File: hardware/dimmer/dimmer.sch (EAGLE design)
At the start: 34 parts, among them IC1 MEGA48/88/168-PU, IC2 RFM12, IC3 7812L, IC4 LP2950Z, K1 G5LE, T1 BC547, T2 BC547, X1 AC In, X2 DIM Out, X3 AC Out

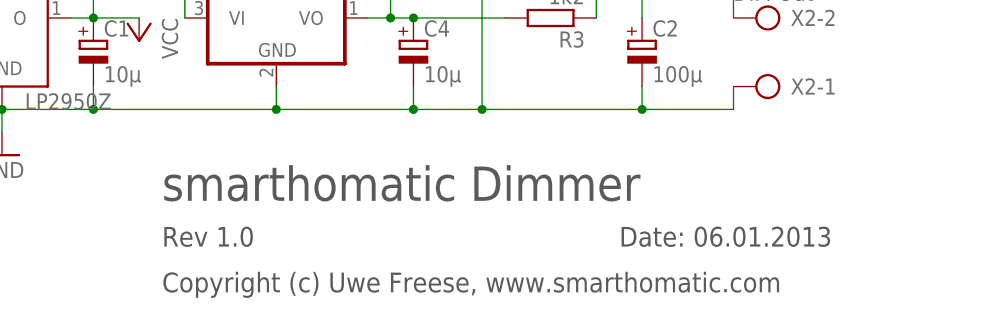
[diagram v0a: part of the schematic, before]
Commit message: use .org domain
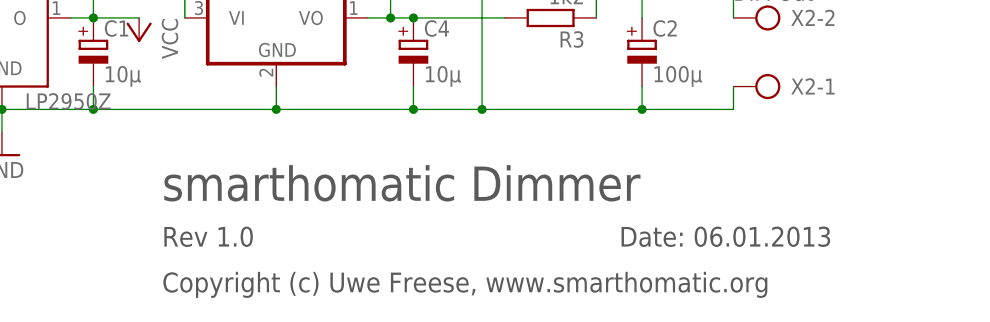
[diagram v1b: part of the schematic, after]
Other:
- note added: "Copyright (c) Uwe Freese, www.smarthomatic.org"
- note removed: "Copyright (c) Uwe Freese, www.smarthomatic.com"
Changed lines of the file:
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@@
 <text x="63.5" y="-81.28" size="2.1844" layer="97">Date: 06.01.2013</text>
 <text x="12.7" y="-81.28" size="2.1844" layer="97">Rev 1.0</text>
-<text x="12.7" y="-86.36" size="2.1844" layer="97">Copyright (c) Uwe Freese, www.smarthomatic.com</text>
+<text x="12.7" y="-86.36" size="2.1844" layer="97">Copyright (c) Uwe Freese, www.smarthomatic.org</text>
 </plain>
 <instances>

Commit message: update labels
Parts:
- D1, D2, D3, D4, D5, D6: value 1N4148DO35-7 -> 1N4148
- JP3: value TX -> PD1/TX
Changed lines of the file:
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@@
 <part name="JP5" library="pinhead" deviceset="PINHD-1X1" device="" value="ANT"/>
 <part name="TR1" library="trafo" deviceset="EE20-1" device="" value="12V"/>
-<part name="D1" library="diode" deviceset="1N4148" device="DO35-7"/>
-<part name="D2" library="diode" deviceset="1N4148" device="DO35-7"/>
-<part name="D3" library="diode" deviceset="1N4148" device="DO35-7"/>
-<part name="D4" library="diode" deviceset="1N4148" device="DO35-7"/>
+<part name="D1" library="diode" deviceset="1N4148" device="DO35-7" value="1N4148"/>
+<part name="D2" library="diode" deviceset="1N4148" device="DO35-7" value="1N4148"/>
+<part name="D3" library="diode" deviceset="1N4148" device="DO35-7" value="1N4148"/>
+<part name="D4" library="diode" deviceset="1N4148" device="DO35-7" value="1N4148"/>
 <part name="IC3" library="linear" deviceset="78*" device="L" technology="12"/>
 <part name="P+4" library="supply1" deviceset="VCC" device=""/>
@@
 <part name="X1" library="con-ptr500" deviceset="AK500/2" device="" value="AC In"/>
 <part name="X2" library="con-ptr500" deviceset="AK500/2" device="" value="DIM Out"/>
-<part name="D5" library="diode" deviceset="1N4148" device="DO35-7"/>
-<part name="D6" library="diode" deviceset="1N4148" device="DO35-7"/>
+<part name="D5" library="diode" deviceset="1N4148" device="DO35-7" value="1N4148"/>
+<part name="D6" library="diode" deviceset="1N4148" device="DO35-7" value="1N4148"/>
 <part name="C4" library="rcl" deviceset="CPOL-EU" device="E1.8-4" value="10µ"/>
 <part name="C3" library="rcl" deviceset="C-EU" device="025-030X050" value="220n"/>
@@
 <part name="R6" library="rcl" deviceset="R-EU_" device="0207/7" value="1k"/>
 <part name="JP2" library="pinhead" deviceset="PINHD-1X2" device="" value="POWER"/>
-<part name="JP3" library="pinhead" deviceset="PINHD-1X1" device="" value="TX"/>
+<part name="JP3" library="pinhead" deviceset="PINHD-1X1" device="" value="PD1/TX"/>
 <part name="JP4" library="pinhead" deviceset="PINHD-1X2" device="" value="On/Off"/>
 <part name="GND4" library="supply1" deviceset="GND" device=""/>

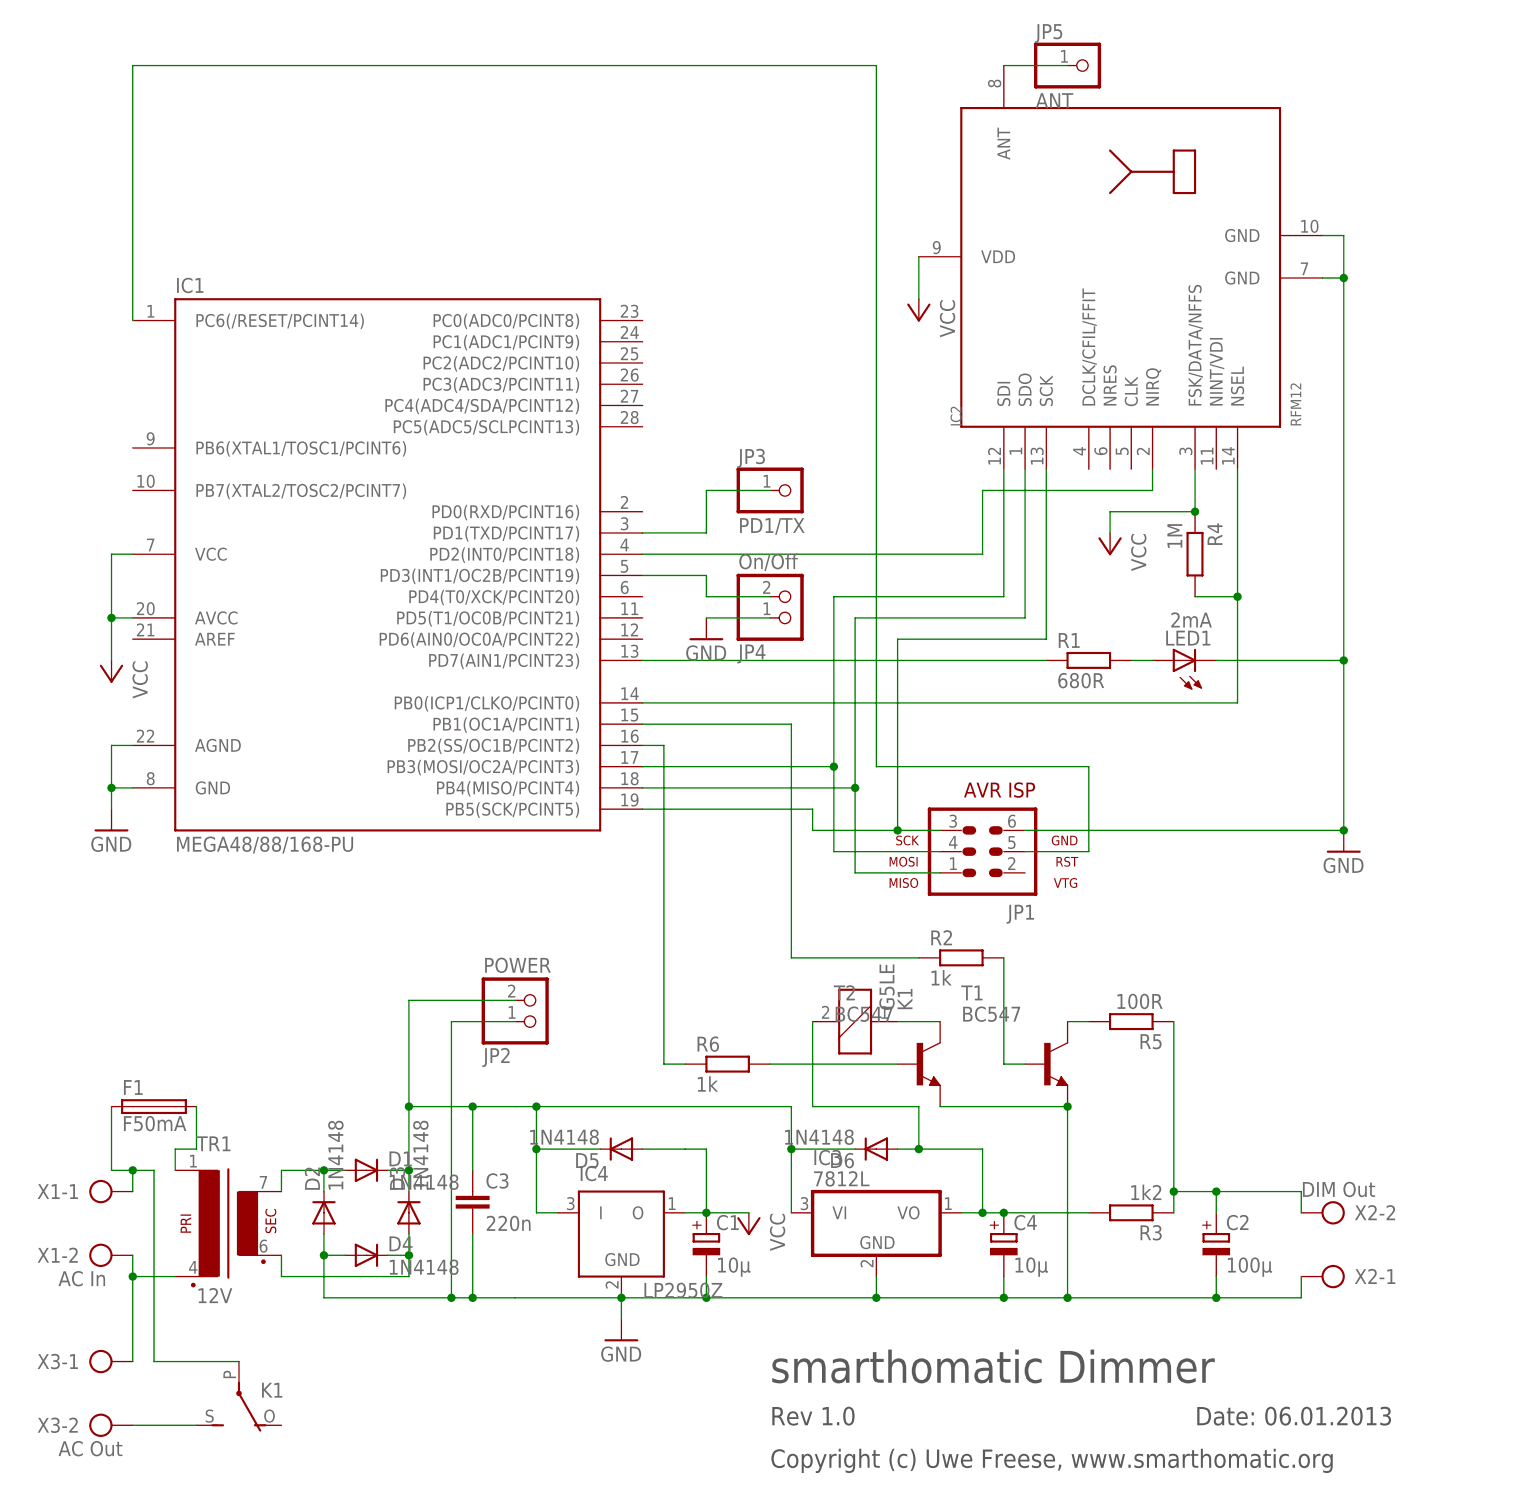
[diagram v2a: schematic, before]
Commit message: Use 1k3 instead of 1k2 resistor (0,1%), which is more common. Adopt lookup table accordingly. Change power off timeout to 3s.
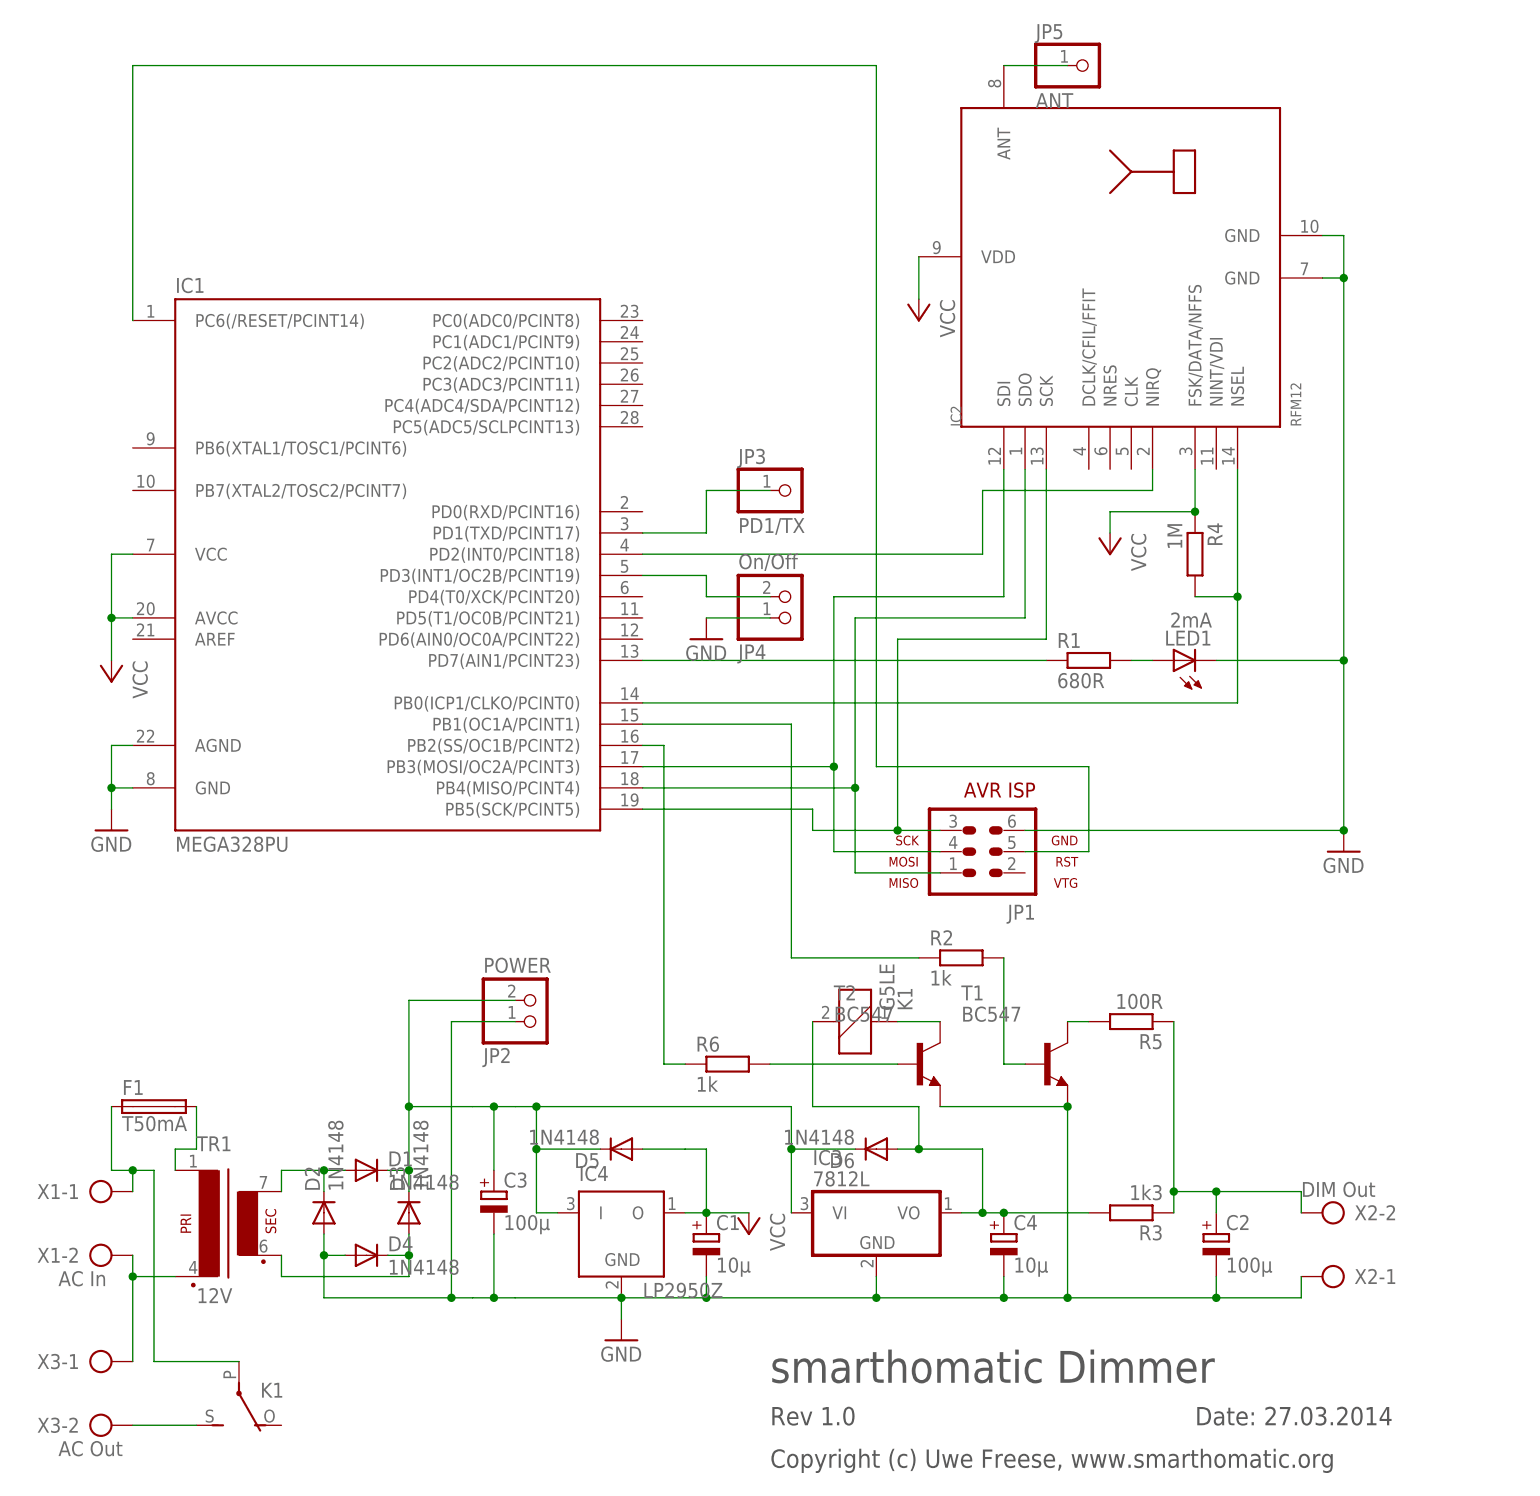
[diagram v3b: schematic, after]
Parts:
- C3: value 220n -> 100µ; device rcl:C-EU025-030X050 -> rcl:CPOL-EUE1.8-4
- F1: value F50mA -> T50mA; device fuse:GSH15 -> fuse:SH22,5
- IC1: value MEGA48/88/168-PU -> MEGA328PU
- R3: value 1k2 -> 1k3
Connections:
- net GND: now also C3.-; no longer C3.2
- net N$9: now also C3.+; no longer C3.1
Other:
- note added: "Date: 27.03.2014"
- note removed: "Date: 06.01.2013"
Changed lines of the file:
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@@
 <part name="IC2" library="hopeRF" deviceset="RFM12" device=""/>
 <part name="LED1" library="led" deviceset="LED" device="3MM" value="2mA"/>
-<part name="IC1" library="avr-5-4.16" deviceset="MEGA48/88/168-PU" device=""/>
+<part name="IC1" library="avr-5-4.16" deviceset="MEGA48/88/168-PU" device="" value="MEGA328PU"/>
 <part name="JP1" library="avr-5-4.16" deviceset="AVR-ISP-6" device=""/>
 <part name="P+1" library="supply1" deviceset="VCC" device=""/>
@@
 <part name="R2" library="rcl" deviceset="R-EU_" device="0207/7" value="1k"/>
 <part name="IC4" library="linear" deviceset="LP2950" device="Z"/>
-<part name="R3" library="rcl" deviceset="R-EU_" device="0207/7" value="1k2"/>
+<part name="R3" library="rcl" deviceset="R-EU_" device="0207/7" value="1k3"/>
 <part name="R5" library="rcl" deviceset="R-EU_" device="0207/7" value="100R"/>
 <part name="C2" library="rcl" deviceset="CPOL-EU" device="E1.8-4" value="100µ"/>
@@
 <part name="D6" library="diode" deviceset="1N4148" device="DO35-7" value="1N4148"/>
 <part name="C4" library="rcl" deviceset="CPOL-EU" device="E1.8-4" value="10µ"/>
-<part name="C3" library="rcl" deviceset="C-EU" device="025-030X050" value="220n"/>
 <part name="X3" library="con-ptr500" deviceset="AK500/2" device="" value="AC Out">
 <attribute name="MF" value=""/>
@@
 </part>
 <part name="K1" library="relay" deviceset="G5LE" device=""/>
-<part name="F1" library="fuse" deviceset="GSH15" device="" value="F50mA"/>
 <part name="T2" library="transistor" deviceset="BC547" device=""/>
 <part name="R6" library="rcl" deviceset="R-EU_" device="0207/7" value="1k"/>
@@
 <part name="JP4" library="pinhead" deviceset="PINHD-1X2" device="" value="On/Off"/>
 <part name="GND4" library="supply1" deviceset="GND" device=""/>
+<part name="F1" library="fuse" deviceset="SH22,5" device="" value="T50mA"/>
+<part name="C3" library="rcl" deviceset="CPOL-EU" device="E1.8-4" value="100µ"/>
 </parts>
 <sheets>
@@
 <frame x1="-81.28" y1="-104.14" x2="99.06" y2="91.44" columns="8" rows="5" layer="97"/>
 <text x="12.7" y="-76.2" size="3.81" layer="97">smarthomatic Dimmer</text>
-<text x="63.5" y="-81.28" size="2.1844" layer="97">Date: 06.01.2013</text>
+<text x="63.5" y="-81.28" size="2.1844" layer="97">Date: 27.03.2014</text>
 <text x="12.7" y="-81.28" size="2.1844" layer="97">Rev 1.0</text>
 <text x="12.7" y="-86.36" size="2.1844" layer="97">Copyright (c) Uwe Freese, www.smarthomatic.org</text>
@@
 <instance part="D6" gate="G$1" x="25.4" y="-48.26" rot="R180"/>
 <instance part="C4" gate="G$1" x="40.64" y="-58.42"/>
-<instance part="C3" gate="G$1" x="-22.86" y="-53.34"/>
 <instance part="X3" gate="-1" x="-68.58" y="-73.66"/>
 <instance part="X3" gate="-2" x="-68.58" y="-81.28"/>
 <instance part="K1" gate="1" x="22.86" y="-33.02" rot="MR90"/>
 <instance part="K1" gate="2" x="-50.8" y="-76.2" rot="MR180"/>
-<instance part="F1" gate="1" x="-60.96" y="-43.18"/>
 <instance part="T2" gate="G$1" x="30.48" y="-38.1"/>
 <instance part="R6" gate="G$1" x="7.62" y="-38.1"/>
@@
 <instance part="JP4" gate="G$1" x="15.24" y="17.78" rot="MR180"/>
 <instance part="GND4" gate="1" x="5.08" y="12.7"/>
+<instance part="F1" gate="1" x="-60.96" y="-43.18"/>
+<instance part="C3" gate="G$1" x="-20.32" y="-53.34"/>
 </instances>
 <busses>
@@
 <wire x1="5.08" y1="-66.04" x2="-5.08" y2="-66.04" width="0.1524" layer="91"/>
 <wire x1="-5.08" y1="-66.04" x2="-17.78" y2="-66.04" width="0.1524" layer="91"/>
-<wire x1="-17.78" y1="-66.04" x2="-22.86" y2="-66.04" width="0.1524" layer="91"/>
+<wire x1="-17.78" y1="-66.04" x2="-20.32" y2="-66.04" width="0.1524" layer="91"/>
+<wire x1="-20.32" y1="-66.04" x2="-22.86" y2="-66.04" width="0.1524" layer="91"/>
 <wire x1="-22.86" y1="-66.04" x2="-25.4" y2="-66.04" width="0.1524" layer="91"/>
 <wire x1="-25.4" y1="-66.04" x2="-40.64" y2="-66.04" width="0.1524" layer="91"/>
@@
 <wire x1="5.08" y1="-66.04" x2="5.08" y2="-63.5" width="0.1524" layer="91"/>
 <junction x="5.08" y="-66.04"/>
-<pinref part="C3" gate="G$1" pin="2"/>
-<wire x1="-22.86" y1="-58.42" x2="-22.86" y2="-66.04" width="0.1524" layer="91"/>
-<junction x="-22.86" y="-66.04"/>
 <pinref part="T2" gate="G$1" pin="E"/>
 <wire x1="33.02" y1="-43.18" x2="48.26" y2="-43.18" width="0.1524" layer="91"/>
@@
 <pinref part="JP2" gate="G$1" pin="1"/>
 <wire x1="-25.4" y1="-33.02" x2="-17.78" y2="-33.02" width="0.1524" layer="91"/>
+<pinref part="C3" gate="G$1" pin="-"/>
+<wire x1="-20.32" y1="-58.42" x2="-20.32" y2="-66.04" width="0.1524" layer="91"/>
+<junction x="-20.32" y="-66.04"/>
 </segment>
 <segment>
@@
 <pinref part="IC3" gate="A1" pin="VI"/>
 <wire x1="-30.48" y1="-43.18" x2="-22.86" y2="-43.18" width="0.1524" layer="91"/>
-<wire x1="-22.86" y1="-43.18" x2="-17.78" y2="-43.18" width="0.1524" layer="91"/>
+<wire x1="-22.86" y1="-43.18" x2="-20.32" y2="-43.18" width="0.1524" layer="91"/>
+<wire x1="-20.32" y1="-43.18" x2="-17.78" y2="-43.18" width="0.1524" layer="91"/>
 <wire x1="-17.78" y1="-43.18" x2="-15.24" y2="-43.18" width="0.1524" layer="91"/>
 <wire x1="-15.24" y1="-43.18" x2="15.24" y2="-43.18" width="0.1524" layer="91"/>
@@
 <wire x1="22.86" y1="-48.26" x2="15.24" y2="-48.26" width="0.1524" layer="91"/>
 <junction x="15.24" y="-48.26"/>
-<pinref part="C3" gate="G$1" pin="1"/>
-<wire x1="-22.86" y1="-50.8" x2="-22.86" y2="-43.18" width="0.1524" layer="91"/>
-<junction x="-22.86" y="-43.18"/>
 <wire x1="-30.48" y1="-43.18" x2="-30.48" y2="-30.48" width="0.1524" layer="91"/>
 <junction x="-30.48" y="-43.18"/>
 <pinref part="JP2" gate="G$1" pin="2"/>
 <wire x1="-30.48" y1="-30.48" x2="-17.78" y2="-30.48" width="0.1524" layer="91"/>
+<pinref part="C3" gate="G$1" pin="+"/>
+<wire x1="-20.32" y1="-43.18" x2="-20.32" y2="-50.8" width="0.1524" layer="91"/>
+<junction x="-20.32" y="-43.18"/>
 </segment>
 </net>
@@
 <segment>
 <wire x1="-63.5" y1="-50.8" x2="-66.04" y2="-50.8" width="0.1524" layer="91"/>
-<pinref part="F1" gate="1" pin="1"/>
-<wire x1="-66.04" y1="-50.8" x2="-66.04" y2="-43.18" width="0.1524" layer="91"/>
 <wire x1="-63.5" y1="-50.8" x2="-60.96" y2="-50.8" width="0.1524" layer="91"/>
 <pinref part="K1" gate="2" pin="P"/>
@@
 <wire x1="-63.5" y1="-53.34" x2="-63.5" y2="-50.8" width="0.1524" layer="91"/>
 <junction x="-63.5" y="-50.8"/>
+<pinref part="F1" gate="1" pin="1"/>
+<wire x1="-66.04" y1="-50.8" x2="-66.04" y2="-43.18" width="0.1524" layer="91"/>
 </segment>
 </net>
 <net name="N$23" class="0">
 <segment>
-<pinref part="F1" gate="1" pin="2"/>
-<wire x1="-55.88" y1="-43.18" x2="-55.88" y2="-48.26" width="0.1524" layer="91"/>
 <wire x1="-55.88" y1="-48.26" x2="-58.42" y2="-48.26" width="0.1524" layer="91"/>
 <pinref part="TR1" gate="1" pin="P1"/>
 <wire x1="-58.42" y1="-48.26" x2="-58.42" y2="-50.8" width="0.1524" layer="91"/>
-</segment>
-</net>
+<pinref part="F1" gate="1" pin="2"/>
+<wire x1="-55.88" y1="-48.26" x2="-55.88" y2="-43.18" width="0.1524" layer="91"/>
+</segment>
+</net>

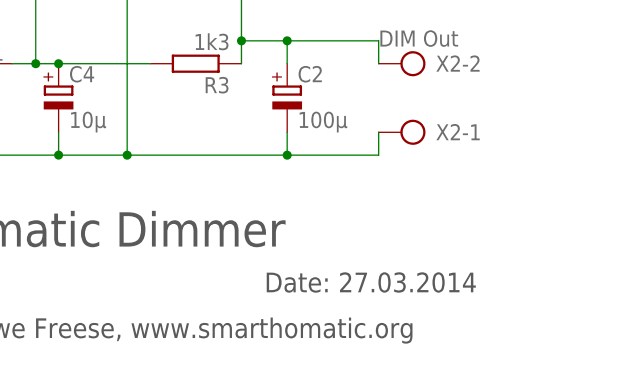
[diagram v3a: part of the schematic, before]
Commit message: minor movement of labels
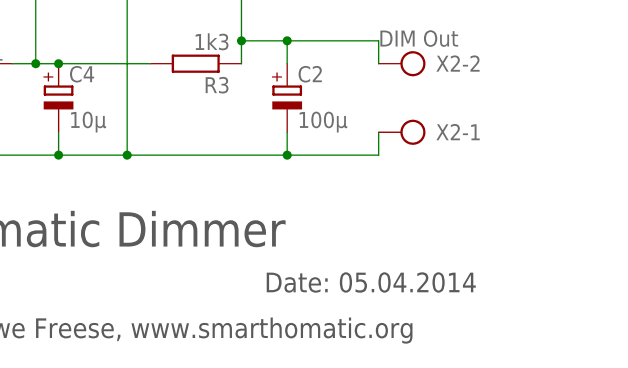
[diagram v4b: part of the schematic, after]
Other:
- note added: "Date: 05.04.2014"
- note removed: "Date: 27.03.2014"
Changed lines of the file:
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@@
 <frame x1="-81.28" y1="-104.14" x2="99.06" y2="91.44" columns="8" rows="5" layer="97"/>
 <text x="12.7" y="-76.2" size="3.81" layer="97">smarthomatic Dimmer</text>
-<text x="63.5" y="-81.28" size="2.1844" layer="97">Date: 27.03.2014</text>
+<text x="63.5" y="-81.28" size="2.1844" layer="97">Date: 05.04.2014</text>
 <text x="12.7" y="-81.28" size="2.1844" layer="97">Rev 1.0</text>
 <text x="12.7" y="-86.36" size="2.1844" layer="97">Copyright (c) Uwe Freese, www.smarthomatic.org</text>
